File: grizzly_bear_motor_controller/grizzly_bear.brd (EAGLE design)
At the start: 71 x 38.9 mm, 56 parts, among them Q1 PH7030L, Q2 PH7030L, Q3 PH7030L, Q4 PH7030L, Q5 FDD4141TO252, U1 A4940, U2 ATMEGA32U4-AU, U3 ACS714, U4 UA78L00, Y1 16MHz

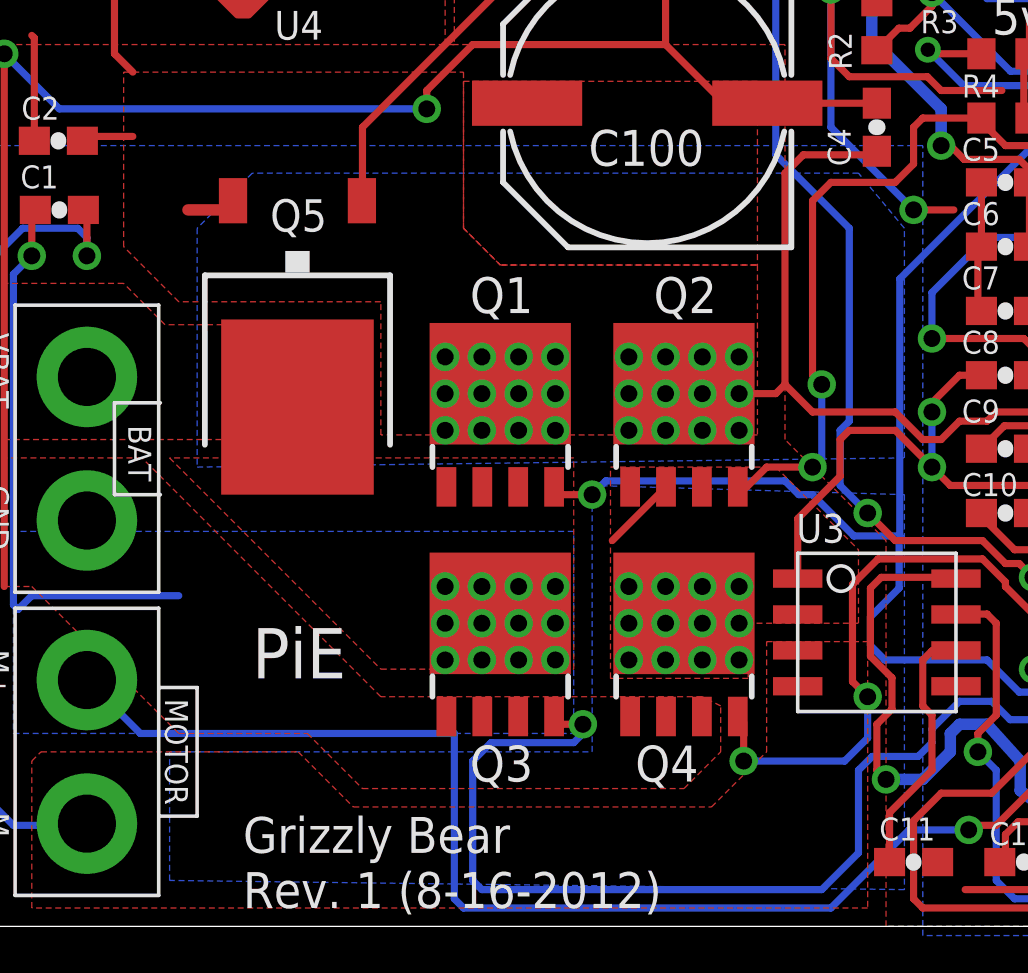
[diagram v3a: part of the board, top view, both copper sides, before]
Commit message: Expand pad on MOSFETs, move MOSFETs apart
Change-Id: Id8161685402c2129cac5230b3d19abb7d14c7031
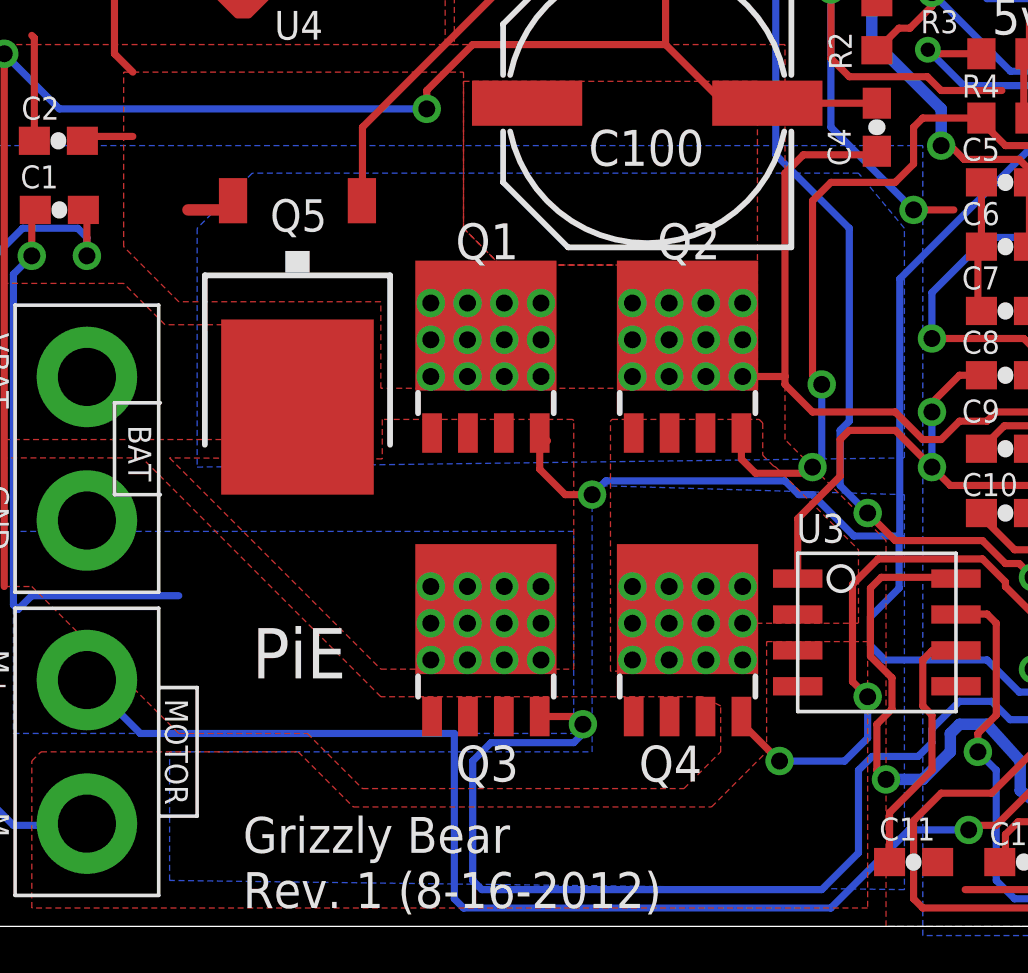
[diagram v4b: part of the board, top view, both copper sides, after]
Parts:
- moved Q1 1.97 mm to (18.0, 18.8)
- moved Q2 1.91 mm to (25.2, 18.8)
- moved Q3 0.51 mm to (18.0, 8.78)
- moved Q4 0.13 mm to (25.2, 8.78)
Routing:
- net SGH: track 45.5 -> 42.6 mm
- net N$2: track 61.5 -> 63.9 mm
- net N$13: track 30.5 -> 31.3 mm
- net N$11: track 74.8 -> 74.0 mm
- net N$8: track 72.9 -> 73.4 mm

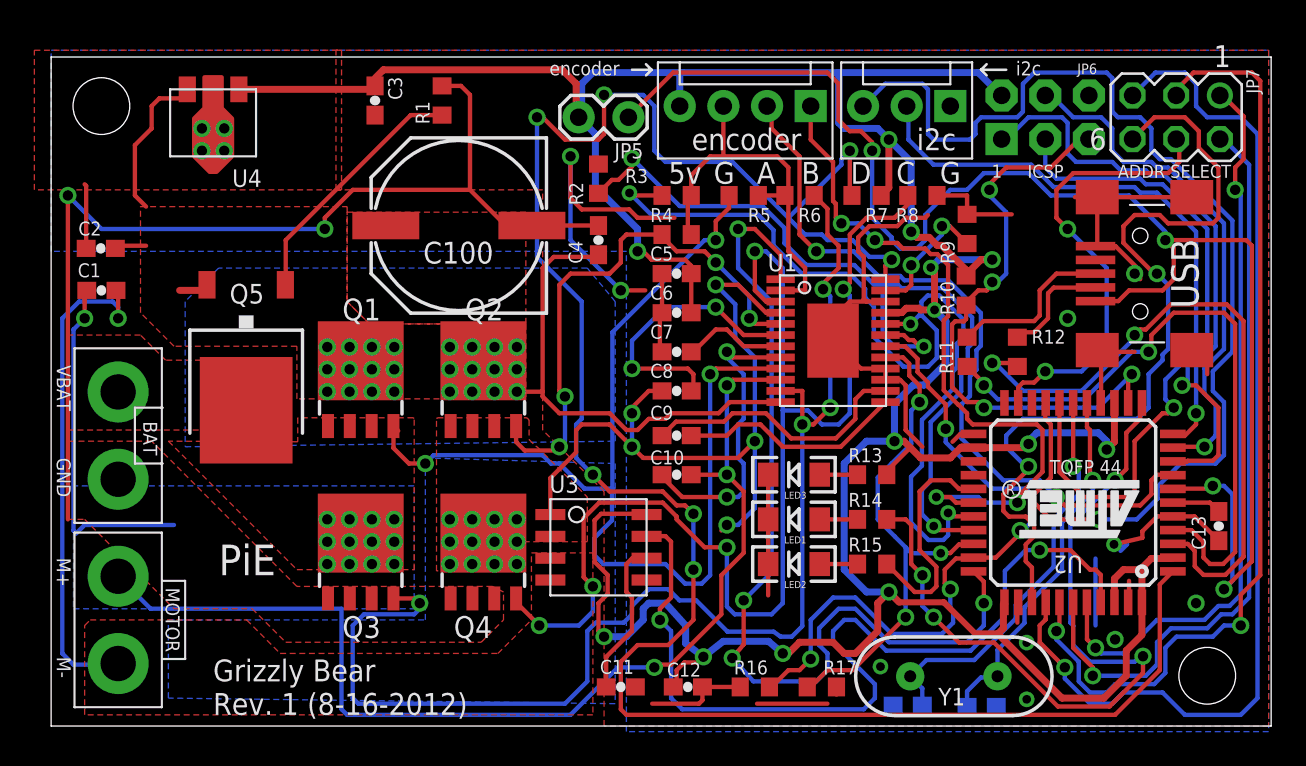
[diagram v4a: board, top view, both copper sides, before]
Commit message: Move via to avoid pad of big capacitor
Change-Id: I1ef2044c39ce79e9cba2cf7a55d8ac52bc4c0fac
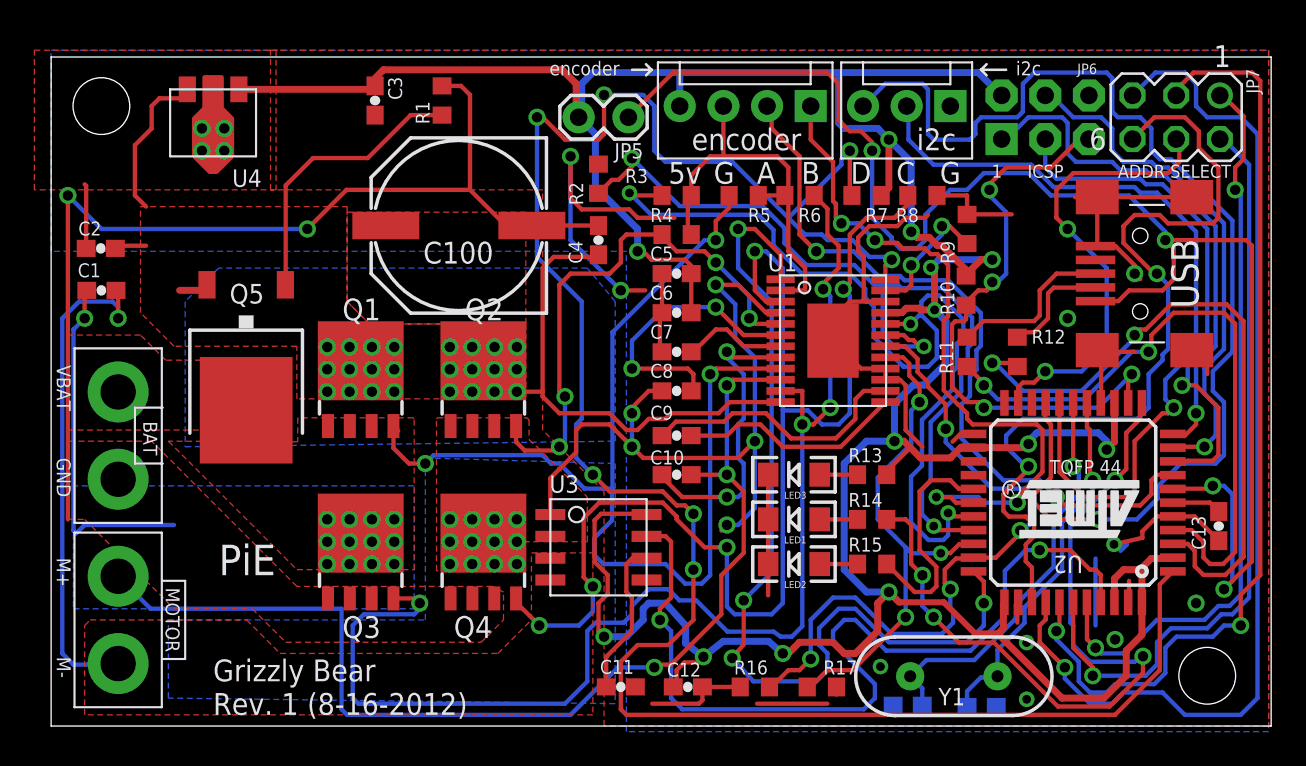
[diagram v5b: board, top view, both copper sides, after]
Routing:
- net N$1: track 14.7 -> 16.6 mm
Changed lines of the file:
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@@
 <layer number="23" name="tOrigins" color="15" fill="1" visible="yes" active="yes"/>
 <layer number="24" name="bOrigins" color="15" fill="1" visible="yes" active="yes"/>
-<layer number="25" name="tNames" color="7" fill="1" visible="no" active="yes"/>
+<layer number="25" name="tNames" color="7" fill="1" visible="yes" active="yes"/>
 <layer number="26" name="bNames" color="12" fill="1" visible="no" active="yes"/>
 <layer number="27" name="tValues" color="7" fill="1" visible="no" active="yes"/>
@@
 <vertex x="28.6" y="15.925"/>
 <vertex x="28.6" y="29.9"/>
-<vertex x="16.575" y="29.9"/>
-<vertex x="16.575" y="38.025"/>
+<vertex x="12.765" y="29.9"/>
+<vertex x="12.765" y="38.025"/>
 <vertex x="70.850003125" y="38.025"/>
 <vertex x="70.850003125" y="-1.3"/>
@@
 <wire x1="2.040003125" y1="30.134996875" x2="1.95" y2="30.225" width="0.254" layer="1"/>
 <polygon width="0.254" layer="1" thermals="no">
-<vertex x="16.9" y="38.025"/>
-<vertex x="16.9" y="29.9"/>
+<vertex x="13.09" y="38.025"/>
+<vertex x="13.09" y="29.9"/>
 <vertex x="-0.975" y="29.9"/>
 <vertex x="-0.975" y="38.025"/>
@@
 <wire x1="26.975" y1="27.3" x2="27.45" y2="27.3" width="0.254" layer="1"/>
 <wire x1="27.45" y1="27.3" x2="27.975" y2="27.825" width="0.254" layer="1"/>
-<via x="15.925" y="27.625" extent="1-16" drill="0.6"/>
+<via x="14.909" y="27.625" extent="1-16" drill="0.6"/>
 <via x="0.975" y="29.575" extent="1-16" drill="0.6"/>
 <wire x1="0.975" y1="29.575" x2="0.975" y2="10.725" width="0.254" layer="1"/>
@@
 <wire x1="23.85" y1="35.95" x2="24.375" y2="35.425" width="0.254" layer="1"/>
 <wire x1="24.375" y1="35.425" x2="24.375" y2="29.9" width="0.254" layer="1"/>
-<wire x1="17.55" y1="29.9" x2="24.375" y2="29.9" width="0.254" layer="1"/>
-<wire x1="17.55" y1="29.9" x2="15.925" y2="28.275" width="0.254" layer="1"/>
-<wire x1="15.925" y1="28.275" x2="15.925" y2="27.625" width="0.254" layer="1"/>
-<wire x1="15.925" y1="27.625" x2="2.925" y2="27.625" width="0.254" layer="16"/>
+<wire x1="17.184" y1="29.9" x2="24.375" y2="29.9" width="0.254" layer="1"/>
 <wire x1="2.925" y1="27.625" x2="0.975" y2="29.575" width="0.254" layer="16"/>
+<wire x1="2.925" y1="27.625" x2="14.909" y2="27.625" width="0.254" layer="16"/>
+<wire x1="17.184" y1="29.9" x2="14.909" y2="27.625" width="0.254" layer="1"/>
 </signal>
 <signal name="N$5">
@@
 <contactref element="R1" pad="2"/>
 <wire x1="22.75" y1="34.25" x2="20.925" y2="34.25" width="0.254" layer="1"/>
-<wire x1="13.65" y1="26.975" x2="13.65" y2="24.395" width="0.254" layer="1"/>
 <wire x1="13.65" y1="24.395" x2="13.63" y2="24.375" width="0.254" layer="1"/>
-<wire x1="20.925" y1="34.25" x2="13.65" y2="26.975" width="0.254" layer="1"/>
+<wire x1="13.65" y1="24.395" x2="13.65" y2="30.16" width="0.254" layer="1"/>
+<wire x1="13.65" y1="30.16" x2="15.24" y2="31.75" width="0.254" layer="1"/>
+<wire x1="15.24" y1="31.75" x2="18.425" y2="31.75" width="0.254" layer="1"/>
+<wire x1="18.425" y1="31.75" x2="20.925" y2="34.25" width="0.254" layer="1"/>
 </signal>
 <signal name="N$7">

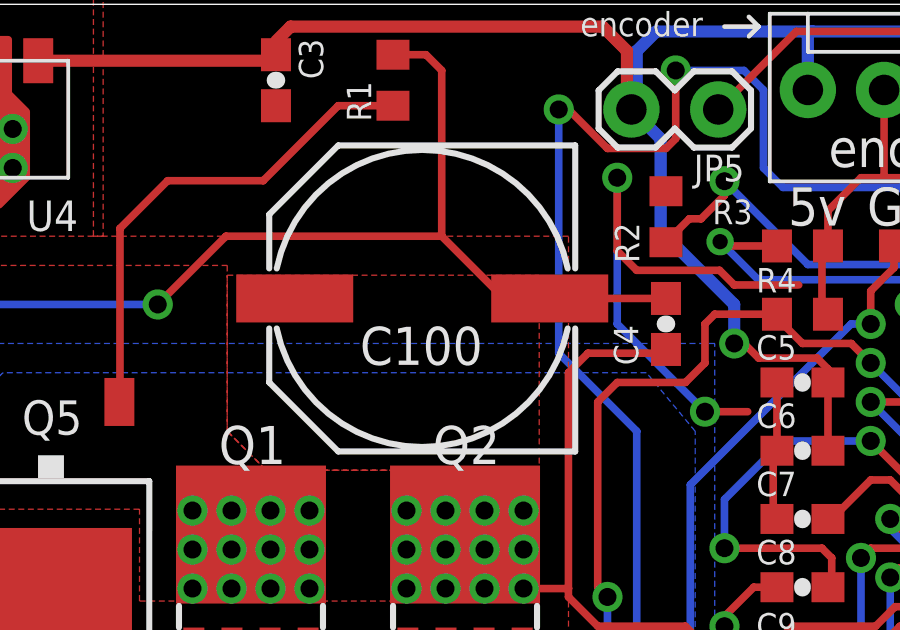
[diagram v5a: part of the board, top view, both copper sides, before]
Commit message: Expand pad of big capacitor
Change-Id: I42f40d14e226f23feeab3faabe0e8d13880d1d3c
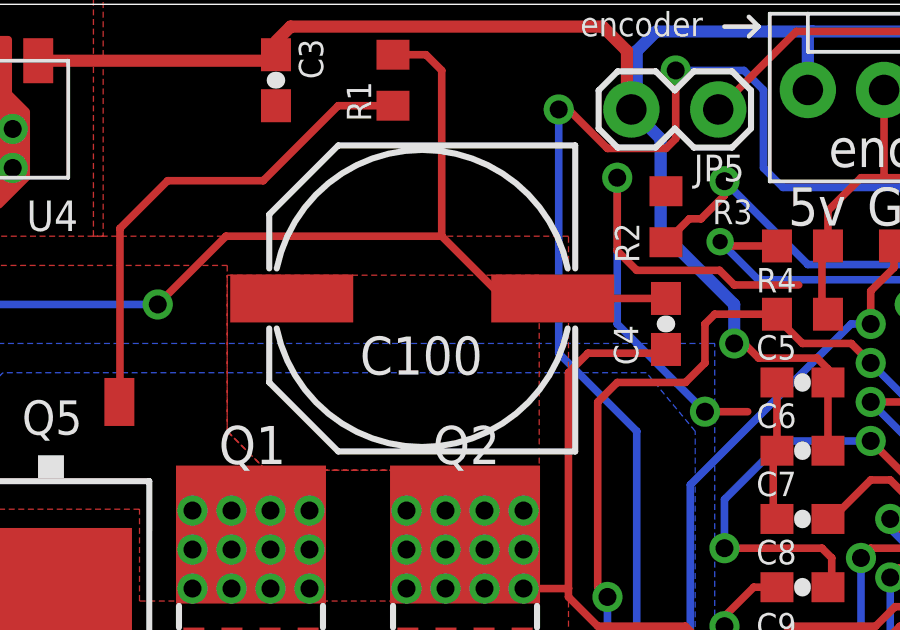
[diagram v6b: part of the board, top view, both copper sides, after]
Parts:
- C100: device SparkFun-Passives:PANASONIC_G -> pie:PANASONIC_G
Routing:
- net BATGND: track 60.2 -> 59.7 mm
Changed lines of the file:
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@@
 <attribute name="VALUE" x="32.4945" y="28.316" size="0.6096" layer="27" font="vector" ratio="15" rot="R270"/>
-</element>
-<element name="C100" library="SparkFun-Passives" package="PANASONIC_G" value="470uF" x="23.725" y="27.825" smashed="yes" rot="R180">
-<attribute name="NAME" x="23.695" y="26.88" size="1.27" layer="25" font="vector" ratio="15" rot="R180" align="bottom-center"/>
-<attribute name="VALUE" x="23.695" y="31.015" size="1.016" layer="27" font="vector" ratio="15" rot="R180" align="bottom-center"/>
 </element>
 <element name="Q5" library="transistor-fet" package="TO252" value="FDD4141TO252" x="11.35" y="19.575" smashed="yes" rot="R180">
@@
 <attribute name="VALUE" x="66.740003125" y="38.316" size="1.27" layer="27" ratio="10" rot="R180"/>
 </element>
+<element name="C100" library="pie" package="PANASONIC_G" value="470uF" x="23.725" y="27.825" smashed="yes" rot="R180">
+<attribute name="NAME" x="23.695" y="26.555" size="1.27" layer="25" font="vector" ratio="15" align="top-center"/>
+<attribute name="VALUE" x="24.995" y="30.365" size="0.4064" layer="27" rot="R180"/>
+</element>
 </elements>
 <signals>
@@
 <contactref element="Q1" pad="MB"/>
 <contactref element="C4" pad="2"/>
-<contactref element="C100" pad="+"/>
 <contactref element="Q5" pad="2"/>
 <contactref element="Q2" pad="MB"/>
@@
 <wire x1="27.102" y1="18.155" x2="28.594" y2="18.155" width="0.254" layer="1"/>
 <wire x1="28.594" y1="18.155" x2="28.6" y2="18.161" width="0.254" layer="1"/>
+<contactref element="C100" pad="+"/>
 </signal>
 <signal name="N$8">
@@
 <contactref element="Q3" pad="2"/>
 <contactref element="C4" pad="1"/>
-<contactref element="C100" pad="-"/>
 <contactref element="Q4" pad="2"/>
 <contactref element="Q4" pad="1"/>
@@
 <vertex x="14.3" y="6.825"/>
 </polygon>
-<wire x1="24.375" y1="29.9" x2="26.975" y2="27.3" width="0.254" layer="1"/>
-<wire x1="26.975" y1="27.3" x2="27.45" y2="27.3" width="0.254" layer="1"/>
-<wire x1="27.45" y1="27.3" x2="27.975" y2="27.825" width="0.254" layer="1"/>
 <via x="14.909" y="27.625" extent="1-16" drill="0.6"/>
 <via x="0.975" y="29.575" extent="1-16" drill="0.6"/>
 <wire x1="0.975" y1="29.575" x2="0.975" y2="10.725" width="0.254" layer="1"/>
-<wire x1="31.85" y1="27.825" x2="28.725" y2="27.825" width="0.254" layer="1"/>
-<wire x1="28.725" y1="27.825" x2="28.6" y2="27.95" width="0.254" layer="1"/>
-<wire x1="28.6" y1="27.95" x2="28.1" y2="27.95" width="0.254" layer="1"/>
-<wire x1="28.1" y1="27.95" x2="27.975" y2="27.825" width="0.254" layer="1"/>
 <wire x1="22.75" y1="35.95" x2="23.85" y2="35.95" width="0.254" layer="1"/>
 <wire x1="23.85" y1="35.95" x2="24.375" y2="35.425" width="0.254" layer="1"/>
@@
 <wire x1="2.925" y1="27.625" x2="14.909" y2="27.625" width="0.254" layer="16"/>
 <wire x1="17.184" y1="29.9" x2="14.909" y2="27.625" width="0.254" layer="1"/>
+<contactref element="C100" pad="-"/>
+<wire x1="28.075" y1="27.825" x2="26.45" y2="27.825" width="0.254" layer="1"/>
+<wire x1="26.45" y1="27.825" x2="24.375" y2="29.9" width="0.254" layer="1"/>
+<wire x1="28.075" y1="27.825" x2="31.85" y2="27.825" width="0.254" layer="1"/>
 </signal>
 <signal name="N$5">
